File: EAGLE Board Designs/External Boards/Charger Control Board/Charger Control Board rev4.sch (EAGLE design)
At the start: 81 parts

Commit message: Made 0805 0603
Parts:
- C1, C2, C3, C4, C5, C6, C7: device HyTechDevices:CAP0805 -> HyTechDevices:CAP0603-CAP
- R1, R10, R11, R12, R13, R14, R15, R16, R17, R18, R19, R2, R20, R26, R27, R28, R29, R3, R30, R31, R34, R35, R36, R4, R5, R6, R7, R8, R9: device HyTechDevices:RESISTOR0805-RES -> HyTechDevices:RESISTOR0603-RES

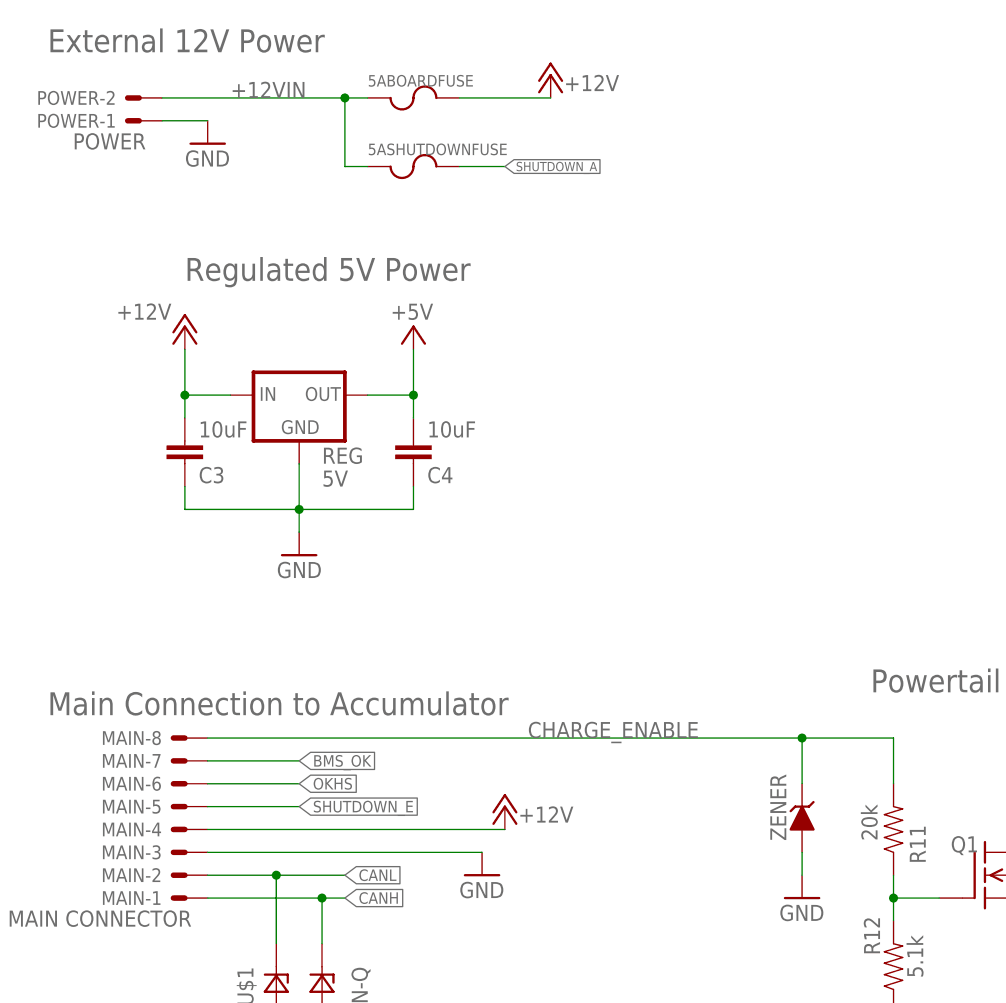
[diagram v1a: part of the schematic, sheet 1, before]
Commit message: Added 0603 zener to protect 12V rail
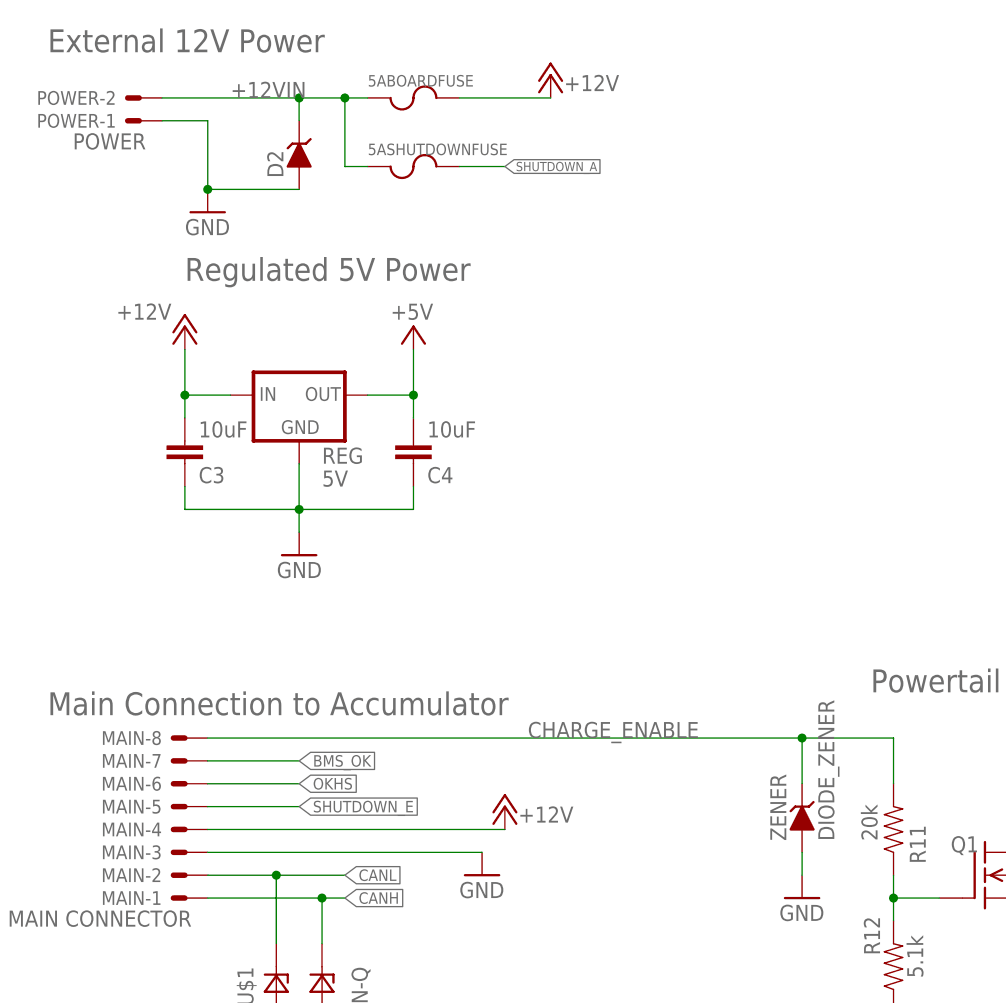
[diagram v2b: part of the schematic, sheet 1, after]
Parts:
- added D2: DIODE_ZENER0603, HyTechDevices:DIODE_ZENER0603
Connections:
- net +12VIN: now also D2.C
- net GND: now also D2.A
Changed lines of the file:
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@@
 </part>
 <part name="GND9" library="HyTechSymbols" deviceset="GND" device=""/>
-<part name="ZENER" library="HyTechDevices" deviceset="DIODE_ZENER" device="" value=""/>
+<part name="ZENER" library="HyTechDevices" deviceset="DIODE_ZENER" device="" value="DIODE_ZENER"/>
 <part name="GND8" library="HyTechSymbols" deviceset="GND" device=""/>
 <part name="Q1" library="HyTechDevices" deviceset="DMG3406L" device="SOT"/>
@@
 <part name="GND22" library="HyTechSymbols" deviceset="GND" device=""/>
 <part name="GND25" library="HyTechSymbols" deviceset="GND" device=""/>
+<part name="D2" library="HyTechDevices" deviceset="DIODE_ZENER" device="0603"/>
 </parts>
 <sheets>
@@
 <attribute name="VALUE" x="43.942" y="244.983" size="1.778" layer="96" rot="R180"/>
 </instance>
-<instance part="GND2" gate="1" x="50.8" y="243.84" smashed="yes">
-<attribute name="VALUE" x="48.26" y="241.3" size="1.778" layer="96"/>
+<instance part="GND2" gate="1" x="50.8" y="236.22" smashed="yes">
+<attribute name="VALUE" x="48.26" y="233.68" size="1.778" layer="96"/>
 </instance>
 <instance part="REG" gate="G$1" x="60.96" y="215.9" smashed="yes">
@@
 <instance part="P+9" gate="1" x="144.78" y="172.72" smashed="yes" rot="MR0">
 <attribute name="VALUE" x="142.24" y="175.26" size="1.778" layer="96" rot="MR180"/>
+</instance>
+<instance part="D2" gate="G$1" x="60.96" y="243.84" smashed="yes" rot="R90">
+<attribute name="NAME" x="59.2074" y="240.03" size="1.778" layer="95" rot="R90"/>
 </instance>
 </instances>
@@
 <segment>
 <pinref part="GND2" gate="1" pin="GND"/>
+<wire x1="50.8" y1="238.76" x2="50.8" y2="246.38" width="0.1524" layer="91"/>
 <wire x1="50.8" y1="246.38" x2="45.72" y2="246.38" width="0.1524" layer="91"/>
 <pinref part="POWER" gate="-1" pin="S"/>
+<pinref part="D2" gate="G$1" pin="A"/>
+<wire x1="50.8" y1="238.76" x2="60.96" y2="238.76" width="0.1524" layer="91"/>
+<junction x="50.8" y="238.76"/>
 </segment>
 <segment>
@@
 <wire x1="66.04" y1="241.3" x2="66.04" y2="248.92" width="0.1524" layer="91"/>
 <pinref part="POWER" gate="-2" pin="S"/>
-<wire x1="66.04" y1="248.92" x2="45.72" y2="248.92" width="0.1524" layer="91"/>
+<wire x1="66.04" y1="248.92" x2="60.96" y2="248.92" width="0.1524" layer="91"/>
 <label x="53.34" y="248.92" size="1.778" layer="95"/>
-</segment>
-</net>
+<pinref part="D2" gate="G$1" pin="C"/>
+<wire x1="60.96" y1="248.92" x2="45.72" y2="248.92" width="0.1524" layer="91"/>
+<wire x1="60.96" y1="246.38" x2="60.96" y2="248.92" width="0.1524" layer="91"/>
+<junction x="60.96" y="248.92"/>
+</segment>
+</net>

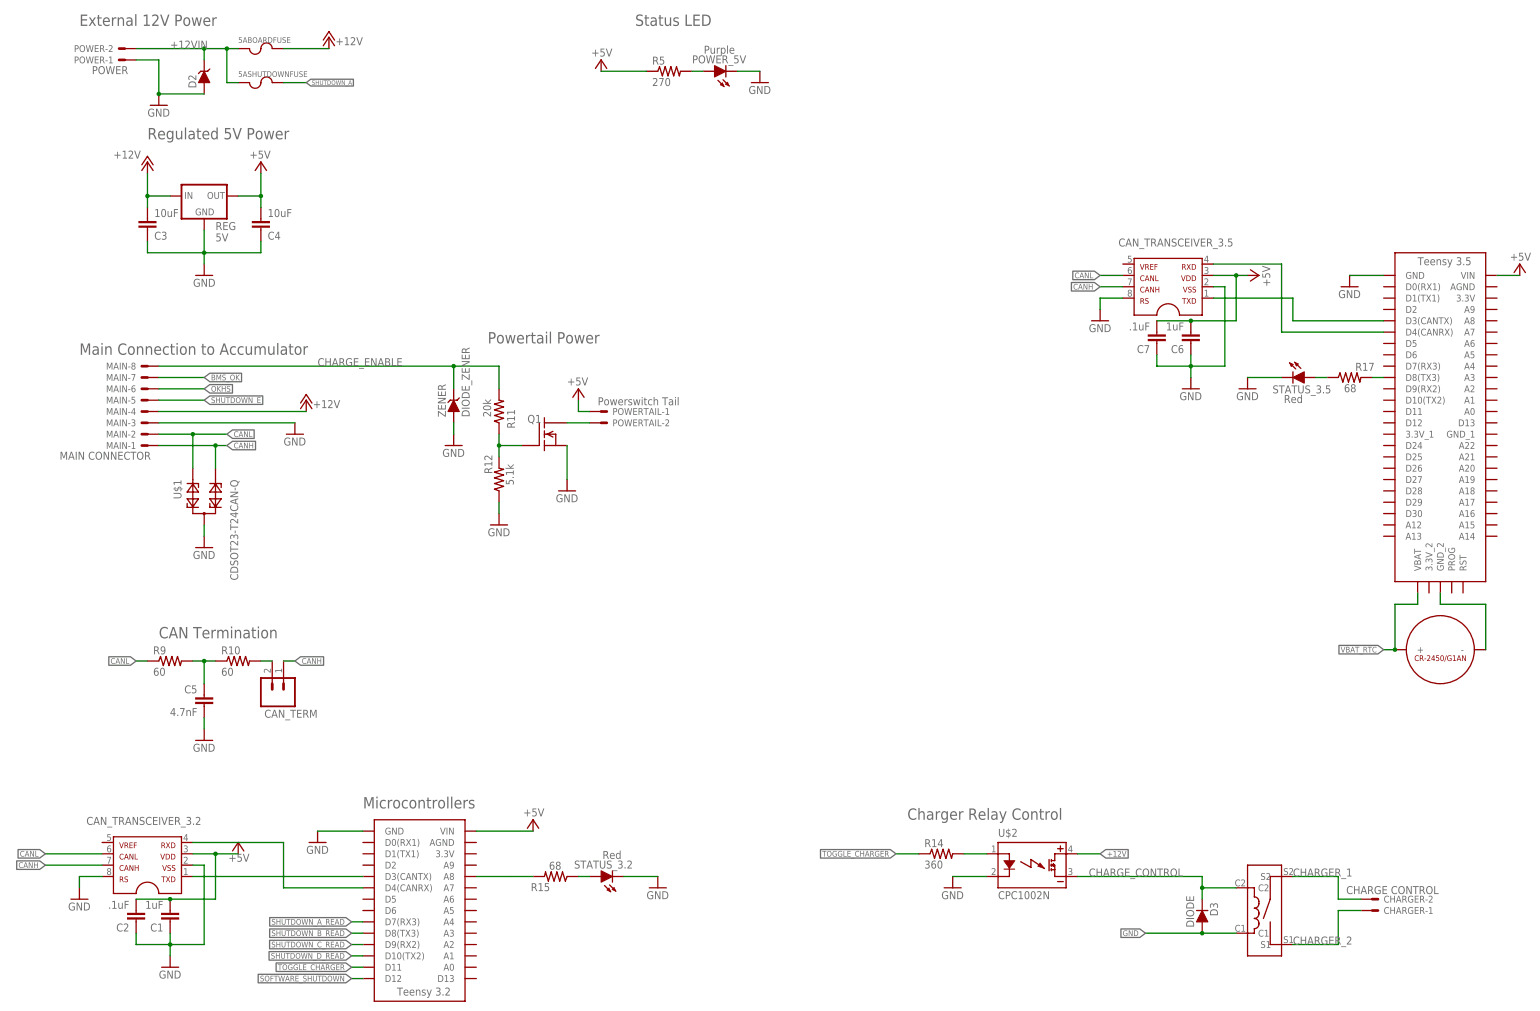
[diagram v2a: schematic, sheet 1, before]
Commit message: Adjusted posistion of componeents and trace widths
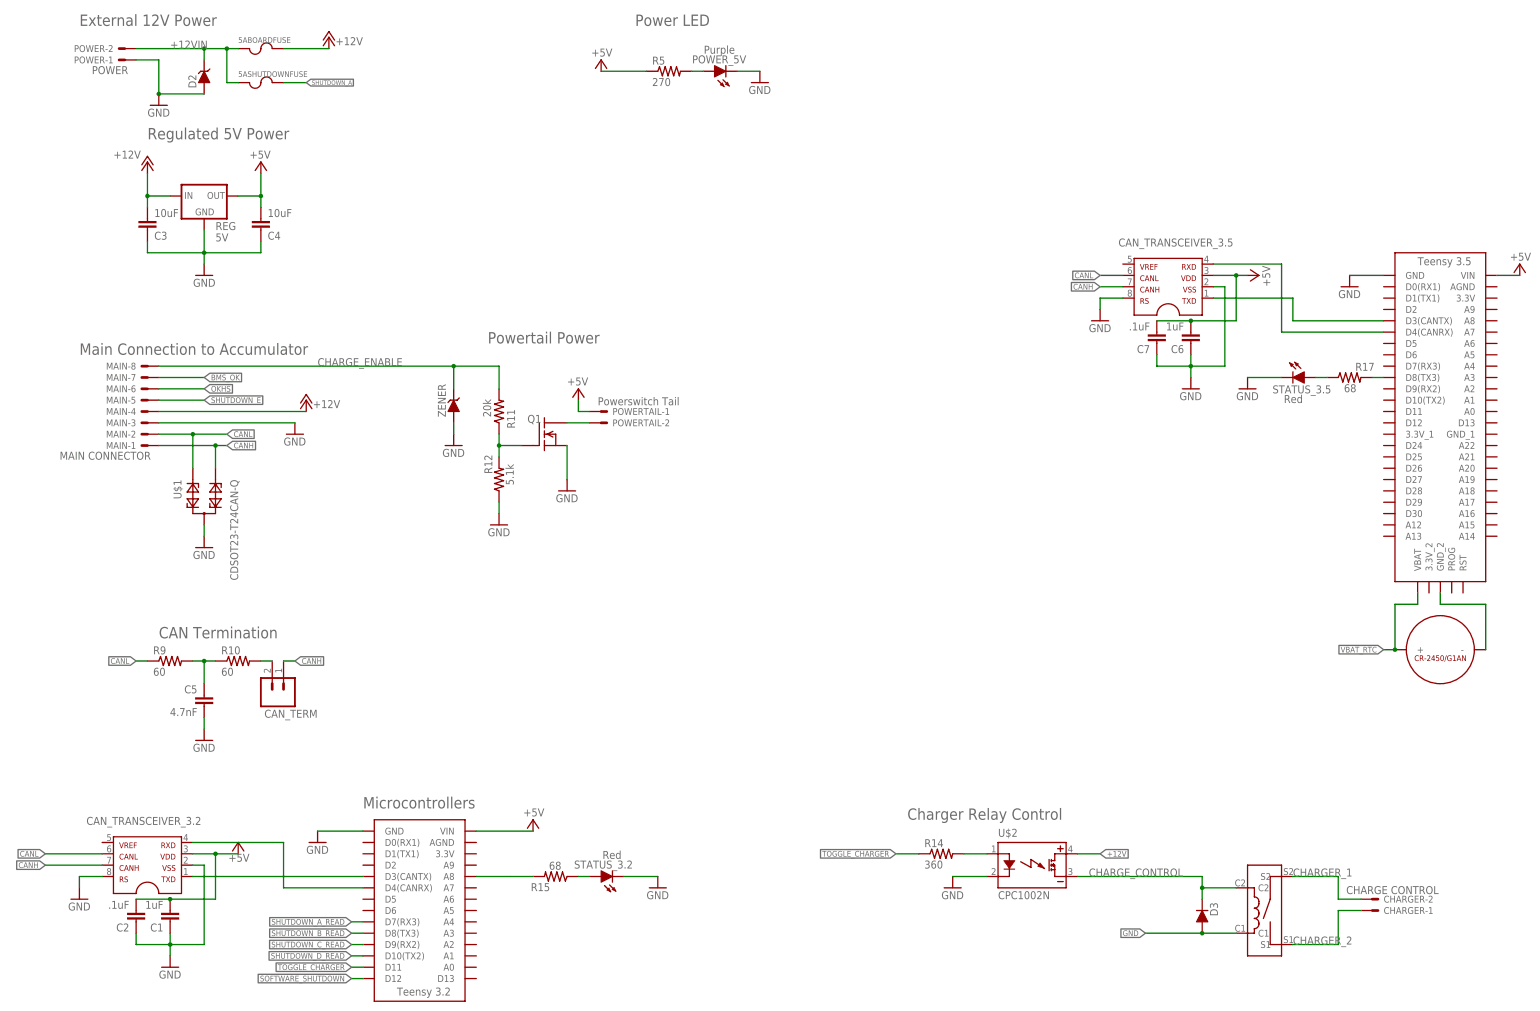
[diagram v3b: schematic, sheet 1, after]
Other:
- note added: "Power LED"
- note removed: "Status LED"
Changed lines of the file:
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@@
 <text x="50.8" y="116.84" size="2.54" layer="95" font="vector">CAN Termination</text>
 <text x="96.52" y="78.74" size="2.54" layer="95" font="vector">Microcontrollers</text>
-<text x="157.48" y="254" size="2.54" layer="95" font="vector">Status LED</text>
+<text x="157.48" y="254" size="2.54" layer="95" font="vector">Power LED</text>
 <text x="33.02" y="254" size="2.54" layer="95" font="vector">External 12V Power</text>
 <text x="48.26" y="228.6" size="2.54" layer="95" font="vector">Regulated 5V Power</text>
@@
 <instance part="ZENER" gate="G$1" x="116.84" y="170.18" smashed="yes" rot="R90">
 <attribute name="NAME" x="115.0874" y="166.37" size="1.778" layer="95" rot="R90"/>
-<attribute name="VALUE" x="120.4214" y="166.37" size="1.778" layer="96" rot="R90"/>
 </instance>
 <instance part="GND8" gate="1" x="116.84" y="160.02" smashed="yes">
@@
 <instance part="D3" gate="1" x="284.48" y="55.88" smashed="yes" rot="MR90">
 <attribute name="NAME" x="286.2326" y="54.61" size="1.778" layer="95" rot="MR90"/>
-<attribute name="VALUE" x="280.8986" y="52.07" size="1.778" layer="96" rot="MR90"/>
 </instance>
 <instance part="U$3" gate="G$1" x="302.26" y="45.72" smashed="yes" rot="R90"/>

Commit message: Adjusted silkscreene
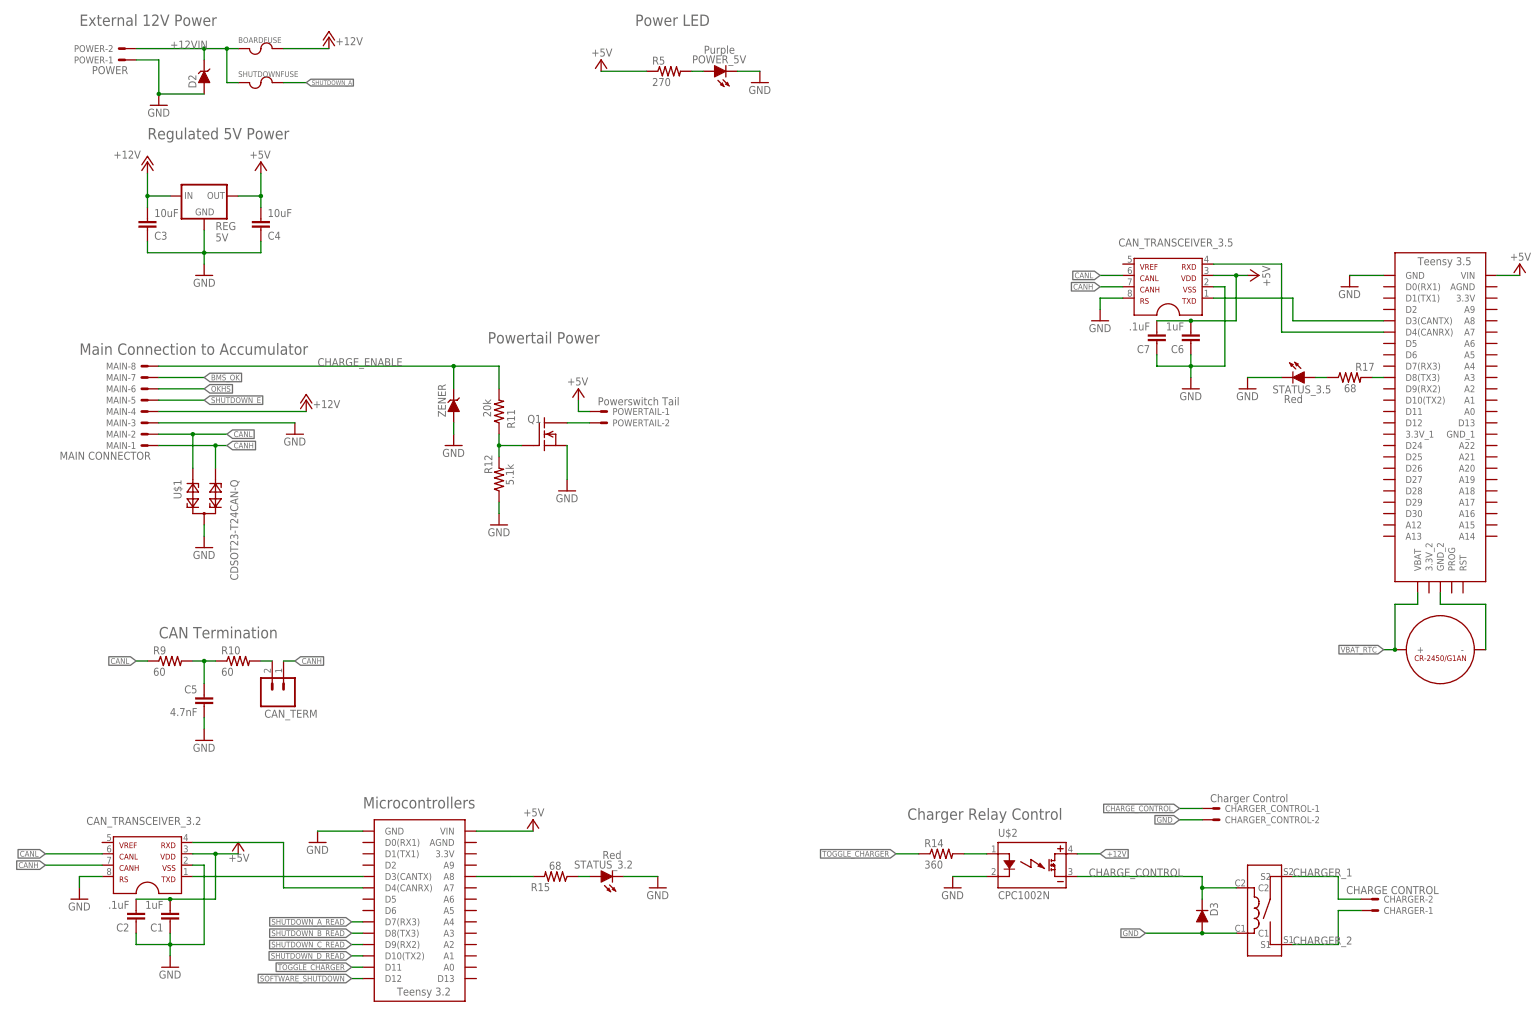
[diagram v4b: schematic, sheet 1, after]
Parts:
- added CHARGER_CONTROL: Charger Control, HyTechDevices:CONNECTOR-2NANO-FIT_VERTICAL-2
- BOARDFUSE: RATING 5A -> 3A
- SHUTDOWNFUSE: RATING 5A -> 4A
- renumbered 5ABOARDFUSE to BOARDFUSE, 5ASHUTDOWNFUSE to SHUTDOWNFUSE
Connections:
- net CHARGE_CONTROL: now also CHARGER_CONTROL-1.S
- net GND: now also CHARGER_CONTROL-2.S
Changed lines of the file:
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@@
 <part name="GND37" library="HyTechSymbols" deviceset="GND" device=""/>
 <part name="U$7" library="HyTechFrames" deviceset="FRAME_B_L" device=""/>
-<part name="5ASHUTDOWNFUSE" library="HyTechDevices" deviceset="FUSE" device="_MINIBLADE">
-<attribute name="RATING" value="5A"/>
+<part name="SHUTDOWNFUSE" library="HyTechDevices" deviceset="FUSE" device="_MINIBLADE">
+<attribute name="RATING" value="4A"/>
 </part>
-<part name="5ABOARDFUSE" library="HyTechDevices" deviceset="FUSE" device="_MINIBLADE">
-<attribute name="RATING" value="5A"/>
+<part name="BOARDFUSE" library="HyTechDevices" deviceset="FUSE" device="_MINIBLADE">
+<attribute name="RATING" value="3A"/>
 </part>
 <part name="P+5" library="supply1" deviceset="+12V" device=""/>
@@
 <part name="GND25" library="HyTechSymbols" deviceset="GND" device=""/>
 <part name="D2" library="HyTechDevices" deviceset="DIODE_ZENER" device="0603"/>
+<part name="CHARGER_CONTROL" library="HyTechDevices" deviceset="CONNECTOR-2" device="NANO-FIT_VERTICAL-2" value="Charger Control"/>
 </parts>
 <sheets>
@@
 <attribute name="DRAWING_NAME" x="356.87" y="22.86" size="2.54" layer="97"/>
 </instance>
-<instance part="5ASHUTDOWNFUSE" gate="G$1" x="73.66" y="241.3" smashed="yes">
+<instance part="SHUTDOWNFUSE" gate="G$1" x="73.66" y="241.3" smashed="yes">
 <attribute name="NAME" x="68.58" y="242.57" size="1.27" layer="95"/>
 <attribute name="VALUE" x="76.2" y="242.57" size="1.27" layer="96"/>
 <attribute name="RATING" x="73.66" y="241.3" size="0.127" layer="96" display="off"/>
 </instance>
-<instance part="5ABOARDFUSE" gate="G$1" x="73.66" y="248.92" smashed="yes">
+<instance part="BOARDFUSE" gate="G$1" x="73.66" y="248.92" smashed="yes">
 <attribute name="NAME" x="68.58" y="250.19" size="1.27" layer="95"/>
 <attribute name="VALUE" x="76.2" y="250.19" size="1.27" layer="96"/>
@@
 <instance part="D2" gate="G$1" x="60.96" y="243.84" smashed="yes" rot="R90">
 <attribute name="NAME" x="59.2074" y="240.03" size="1.778" layer="95" rot="R90"/>
+</instance>
+<instance part="CHARGER_CONTROL" gate="-2" x="287.02" y="76.2" smashed="yes">
+<attribute name="NAME" x="289.56" y="75.438" size="1.524" layer="95"/>
+</instance>
+<instance part="CHARGER_CONTROL" gate="-1" x="287.02" y="78.74" smashed="yes">
+<attribute name="NAME" x="289.56" y="77.978" size="1.524" layer="95"/>
+<attribute name="VALUE" x="286.258" y="80.137" size="1.778" layer="96"/>
 </instance>
 </instances>
@@
 <wire x1="48.26" y1="203.2" x2="60.96" y2="203.2" width="0.1524" layer="91"/>
 </segment>
+<segment>
+<pinref part="CHARGER_CONTROL" gate="-2" pin="S"/>
+<wire x1="284.48" y1="76.2" x2="279.4" y2="76.2" width="0.1524" layer="91"/>
+<label x="279.4" y="76.2" size="1.27" layer="95" font="vector" rot="R180" xref="yes"/>
+</segment>
 </net>
 <net name="CANH" class="0">
@@
 <wire x1="292.1" y1="60.96" x2="284.48" y2="60.96" width="0.1524" layer="91"/>
 <junction x="284.48" y="60.96"/>
+</segment>
+<segment>
+<pinref part="CHARGER_CONTROL" gate="-1" pin="S"/>
+<wire x1="284.48" y1="78.74" x2="279.4" y2="78.74" width="0.1524" layer="91"/>
+<label x="279.4" y="78.74" size="1.27" layer="95" font="vector" rot="R180" xref="yes"/>
 </segment>
 </net>
@@
 </segment>
 <segment>
-<pinref part="5ABOARDFUSE" gate="G$1" pin="2"/>
+<pinref part="BOARDFUSE" gate="G$1" pin="2"/>
 <wire x1="78.74" y1="248.92" x2="88.9" y2="248.92" width="0.1524" layer="91"/>
 <pinref part="P+5" gate="1" pin="+12V"/>
@@
 <net name="SHUTDOWN_A" class="0">
 <segment>
-<pinref part="5ASHUTDOWNFUSE" gate="G$1" pin="2"/>
+<pinref part="SHUTDOWNFUSE" gate="G$1" pin="2"/>
 <wire x1="78.74" y1="241.3" x2="83.82" y2="241.3" width="0.1524" layer="91"/>
 <label x="83.82" y="241.3" size="1.016" layer="95" xref="yes"/>
@@
 <net name="+12VIN" class="0">
 <segment>
-<pinref part="5ASHUTDOWNFUSE" gate="G$1" pin="1"/>
-<pinref part="5ABOARDFUSE" gate="G$1" pin="1"/>
+<pinref part="SHUTDOWNFUSE" gate="G$1" pin="1"/>
+<pinref part="BOARDFUSE" gate="G$1" pin="1"/>
 <wire x1="66.04" y1="248.92" x2="68.58" y2="248.92" width="0.1524" layer="91"/>
 <junction x="66.04" y="248.92"/>
